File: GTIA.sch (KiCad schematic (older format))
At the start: 71 parts, among them J2 Video, Q1 2N3904, Q2 2N3904, Q3 2N3904, Q6 2N3904, U17 GTIA, U18 74LS08, U20 4050, U21 74LS74, Y2 4,43 MHz

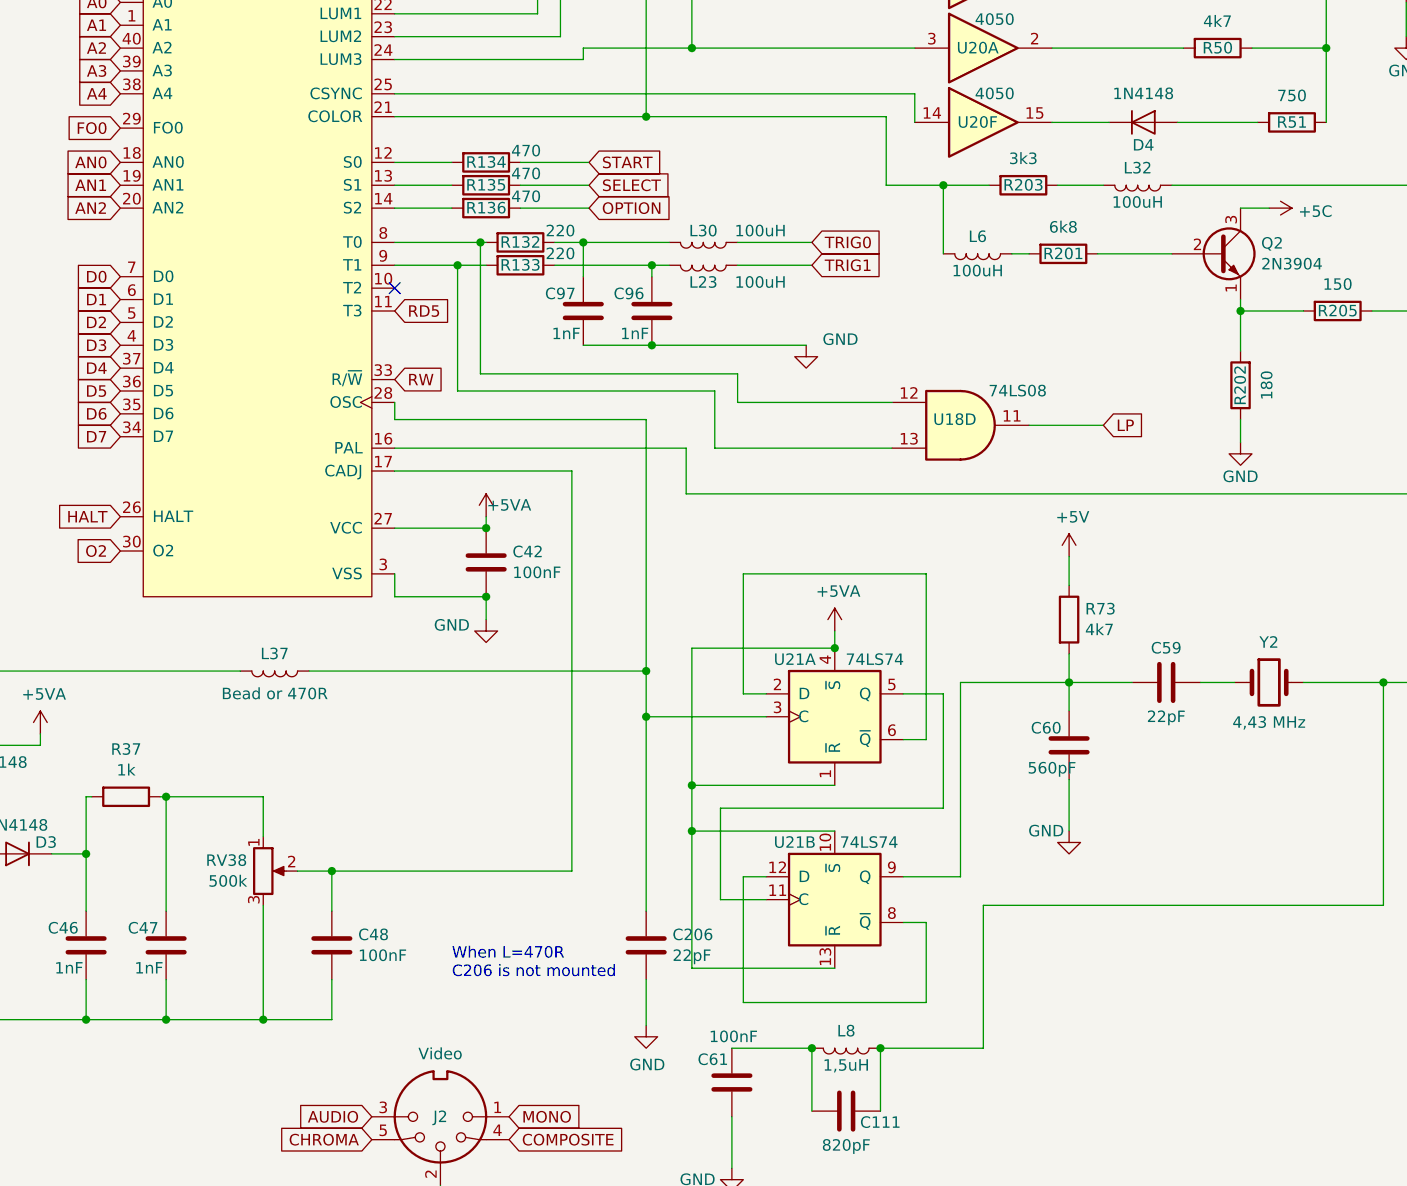
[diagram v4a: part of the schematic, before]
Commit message: Audio put on board
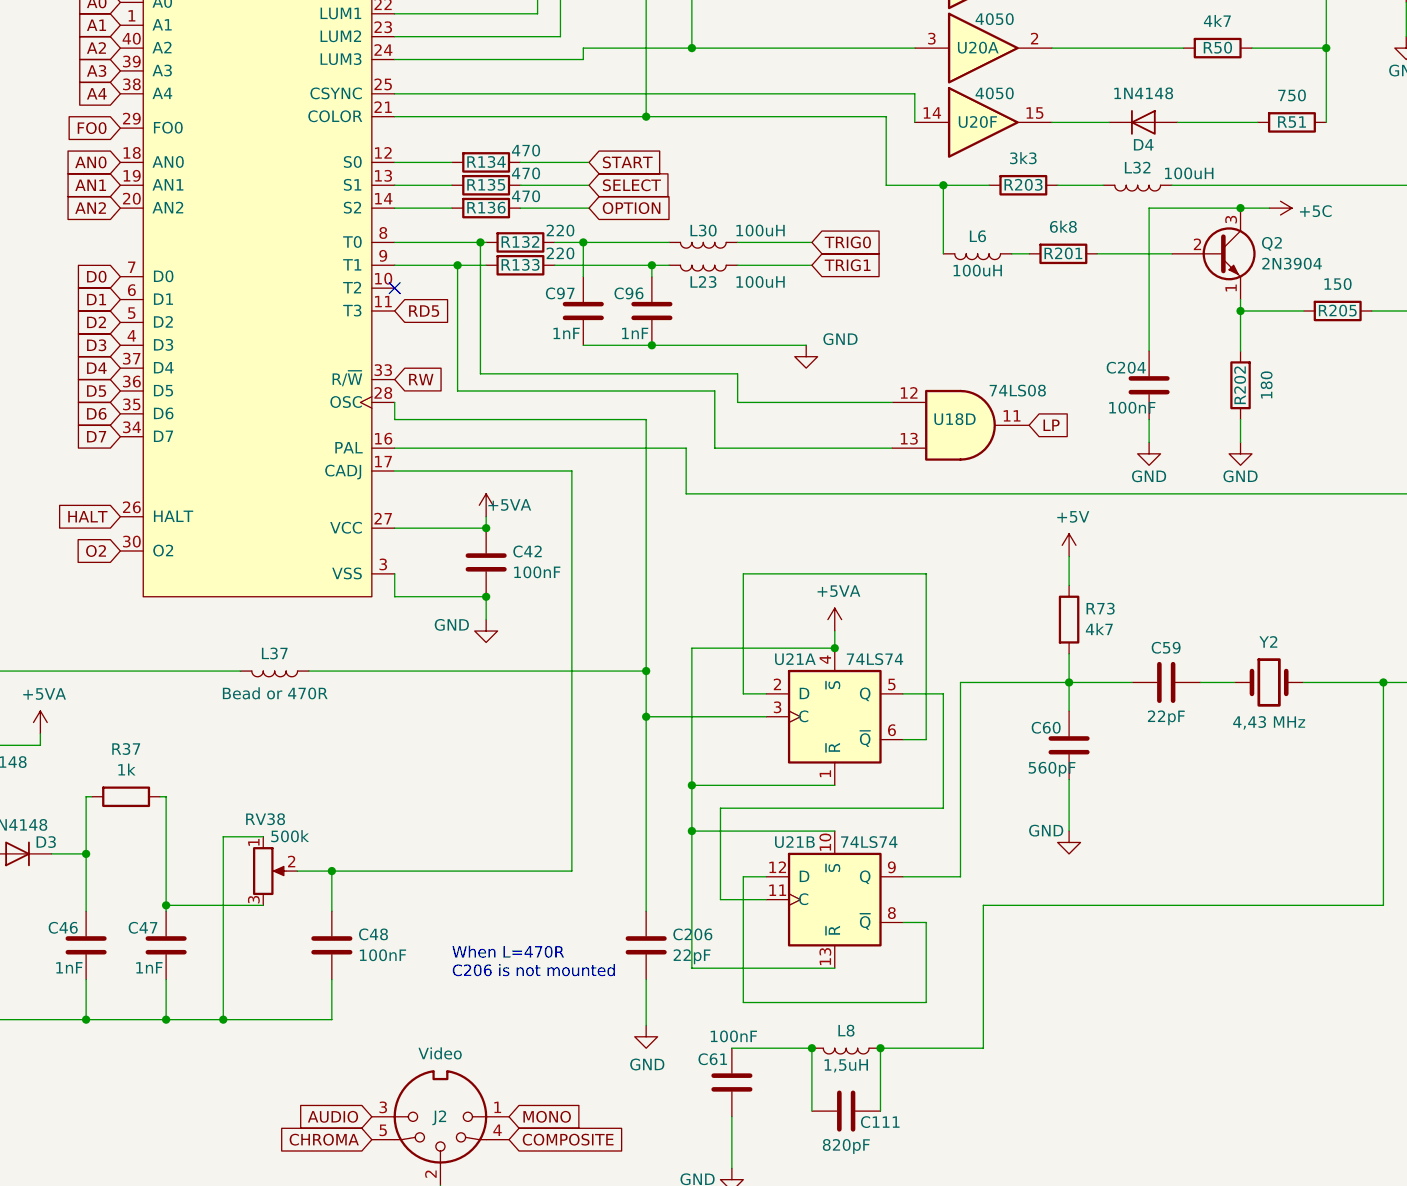
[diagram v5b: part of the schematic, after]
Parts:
- added C204: 100nF, Atari:C_Axial_L5.1mm_D2.5mm_P12.50mm_Horizontal, symbol Device:C
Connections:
- net +5C: now also C204.2
- net GND: now also RV38.1, C204.1; no longer RV38.3
- net at C47.2, R37.1: now also RV38.3; no longer RV38.1
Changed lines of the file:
@@
 Connection ~ 2975 6000
 Wire Wire Line
-	3325 5750 3325 6250
+	3325 5750 3325 6225
 Wire Wire Line
 	3325 5750 3300 5750
@@
 U 1 1 602637FB
 P 3750 6075
-F 0 "RV38" H 3680 6121 50  0000 R CNN
-F 1 "500k" H 3680 6030 50  0000 R CNN
+F 0 "RV38" H 3850 6300 50  0000 R CNN
+F 1 "500k" H 3950 6225 50  0000 R CNN
 F 2 "Potentiometer_THT:Potentiometer_ACP_CA9-V10_Vertical_Hole" H 3750 6075 50  0001 C CNN
 F 3 "~" H 3750 6075 50  0001 C CNN
@@
 	1    0    0    -1
 $EndComp
-Wire Wire Line
-	3325 5750 3750 5750
-Wire Wire Line
-	3750 5750 3750 5925
-Connection ~ 3325 5750
 $Comp
 L Device:C C48
@@
 Wire Wire Line
 	4050 6550 4050 6725
-Wire Wire Line
-	4050 6725 3750 6725
 Connection ~ 1600 6725
 Wire Wire Line
 	1600 6725 1600 6750
-Wire Wire Line
-	3750 6225 3750 6725
-Connection ~ 3750 6725
-Wire Wire Line
-	3750 6725 3325 6725
 Wire Wire Line
 	3325 6550 3325 6725
@@
 P 7575 3075
 F 0 "L32" V 7500 3075 50  0000 C CNN
-F 1 "100uH" V 7650 3075 50  0000 C CNN
+F 1 "100uH" V 7525 3300 50  0000 C CNN
 F 2 "Atari:L_Axial_L7.0mm_D3.3mm_P12.50mm_Horizontal_Fastron_MICC" H 7575 3075 50  0001 C CNN
 F 3 "~" H 7575 3075 50  0001 C CNN
@@
 Wire Wire Line
 	4600 3425 4725 3425
-Text GLabel 7425 4125 2    50   Input ~ 0
+Text GLabel 7100 4125 2    50   Input ~ 0
 LP
-Wire Wire Line
-	7100 4125 7425 4125
 Wire Wire Line
 	5150 3475 5150 3325
@@
 	1    0    0    -1
 $EndComp
+$Comp
+L Device:C C204
+U 1 1 60308154
+P 7625 3950
+F 0 "C204" H 7725 3875 50  0000 C CNN
+F 1 "100nF" H 7700 4050 50  0000 C CNN
+F 2 "Atari:C_Axial_L5.1mm_D2.5mm_P12.50mm_Horizontal" H 7663 3800 50  0001 C CNN
+F 3 "~" H 7625 3950 50  0001 C CNN
+	1    7625 3950
+	-1   0    0    1
+$EndComp
+$Comp
+L power:GND #PWR0248
+U 1 1 60308DC4
+P 7625 4200
+F 0 "#PWR0248" H 7625 3950 50  0001 C CNN
+F 1 "GND" H 7625 4050 50  0000 C CNN
+F 2 "" H 7625 4200 50  0001 C CNN
+F 3 "" H 7625 4200 50  0001 C CNN
+	1    7625 4200
+	1    0    0    -1
+$EndComp
+Wire Wire Line
+	7625 4100 7625 4200
+Wire Wire Line
+	7625 3800 7625 3175
+Wire Wire Line
+	7625 3175 8025 3175
+Connection ~ 8025 3175
+Wire Wire Line
+	3325 6725 3575 6725
+Wire Wire Line
+	3750 5925 3575 5925
+Wire Wire Line
+	3575 5925 3575 6725
+Connection ~ 3575 6725
+Wire Wire Line
+	3575 6725 4050 6725
+Wire Wire Line
+	3750 6225 3325 6225
+Connection ~ 3325 6225
+Wire Wire Line
+	3325 6225 3325 6250
 $EndSCHEMATC

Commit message: Patching
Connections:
- net +5V: no longer R73.1
- net +5VA: now also R73.1
- net GND: now also C58.2, U21.7 (GND)
- net at C59.2: now also Y2.2; no longer Y2.1
- net at C111.1, L8.1, R71.2: now also Y2.1; no longer Y2.2
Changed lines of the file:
@@
 F 3 "~" H 8150 5250 50  0001 C CNN
 	1    8150 5250
-	1    0    0    -1
+	-1   0    0    1
 $EndComp
 $Comp
@@
 $EndComp
 $Comp
-L power:+5V #PWR0166
-U 1 1 602CB043
-P 7275 4700
-F 0 "#PWR0166" H 7275 4550 50  0001 C CNN
-F 1 "+5V" H 7290 4873 50  0000 C CNN
-F 2 "" H 7275 4700 50  0001 C CNN
-F 3 "" H 7275 4700 50  0001 C CNN
-	1    7275 4700
-	1    0    0    -1
-$EndComp
-$Comp
 L Device:C C204
 U 1 1 60308154
@@
 Wire Wire Line
 	3325 6225 3325 6250
+$Comp
+L power:GND #PWR0249
+U 1 1 6034B9B1
+P 1050 4200
+F 0 "#PWR0249" H 1050 3950 50  0001 C CNN
+F 1 "GND" H 900 4175 50  0000 C CNN
+F 2 "" H 1050 4200 50  0001 C CNN
+F 3 "" H 1050 4200 50  0001 C CNN
+	1    1050 4200
+	1    0    0    -1
+$EndComp
+$Comp
+L power:+5VA #PWR0166
+U 1 1 6035DAC7
+P 7275 4700
+F 0 "#PWR0166" H 7275 4550 50  0001 C CNN
+F 1 "+5VA" H 7290 4873 50  0000 C CNN
+F 2 "" H 7275 4700 50  0001 C CNN
+F 3 "" H 7275 4700 50  0001 C CNN
+	1    7275 4700
+	1    0    0    -1
+$EndComp
 $EndSCHEMATC

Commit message: Tracking
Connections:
- net at C46.2, D3.1 (K): now also R37.1; no longer R37.2
- net at C47.2, RV38.3: now also R37.2; no longer R37.1
- net MONO_MOD: now reaches Q3.1 (E), R204.2, R53.1
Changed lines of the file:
@@
 F 3 "~" H 3150 5750 50  0001 C CNN
 	1    3150 5750
-	0    1    1    0
+	0    -1   -1   0
 $EndComp
 Wire Wire Line
@@
 	9300 2275 9300 2425
 Wire Wire Line
-	9675 1900 9300 1900
+	9675 1900 9600 1900
 Connection ~ 9300 1900
 Wire Wire Line
@@
 	1    0    0    -1
 $EndComp
+Text GLabel 10425 2300 2    50   Input ~ 0
+MONO_MOD
+Wire Wire Line
+	10425 2300 9600 2300
+Wire Wire Line
+	9600 2300 9600 1900
+Connection ~ 9600 1900
+Wire Wire Line
+	9600 1900 9300 1900
 $EndSCHEMATC

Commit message: Tracking
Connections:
- net +5V is gone; now on net +5VA: R72.1
- net O2 renamed BO2
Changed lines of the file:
@@
 HALT
 Text GLabel 3125 4675 0    50   Input ~ 0
-O2
+BO2
 Text GLabel 3125 2075 0    50   Input ~ 0
 GTIA
@@
 MONO
 $Comp
-L power:+5V #PWR0163
-U 1 1 602CA007
-P 10050 4350
-F 0 "#PWR0163" H 10050 4200 50  0001 C CNN
-F 1 "+5V" H 10065 4523 50  0000 C CNN
-F 2 "" H 10050 4350 50  0001 C CNN
-F 3 "" H 10050 4350 50  0001 C CNN
-	1    10050 4350
-	1    0    0    -1
-$EndComp
-$Comp
 L Device:C C204
 U 1 1 60308154
@@
 Wire Wire Line
 	9600 1900 9300 1900
+$Comp
+L power:+5VA #PWR0163
+U 1 1 6036AA54
+P 10050 4350
+F 0 "#PWR0163" H 10050 4200 50  0001 C CNN
+F 1 "+5VA" H 10065 4523 50  0000 C CNN
+F 2 "" H 10050 4350 50  0001 C CNN
+F 3 "" H 10050 4350 50  0001 C CNN
+	1    10050 4350
+	1    0    0    -1
+$EndComp
 $EndSCHEMATC
